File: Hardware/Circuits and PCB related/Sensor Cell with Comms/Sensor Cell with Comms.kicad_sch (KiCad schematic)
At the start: 3 parts, among them U12 STM32F103C6T6

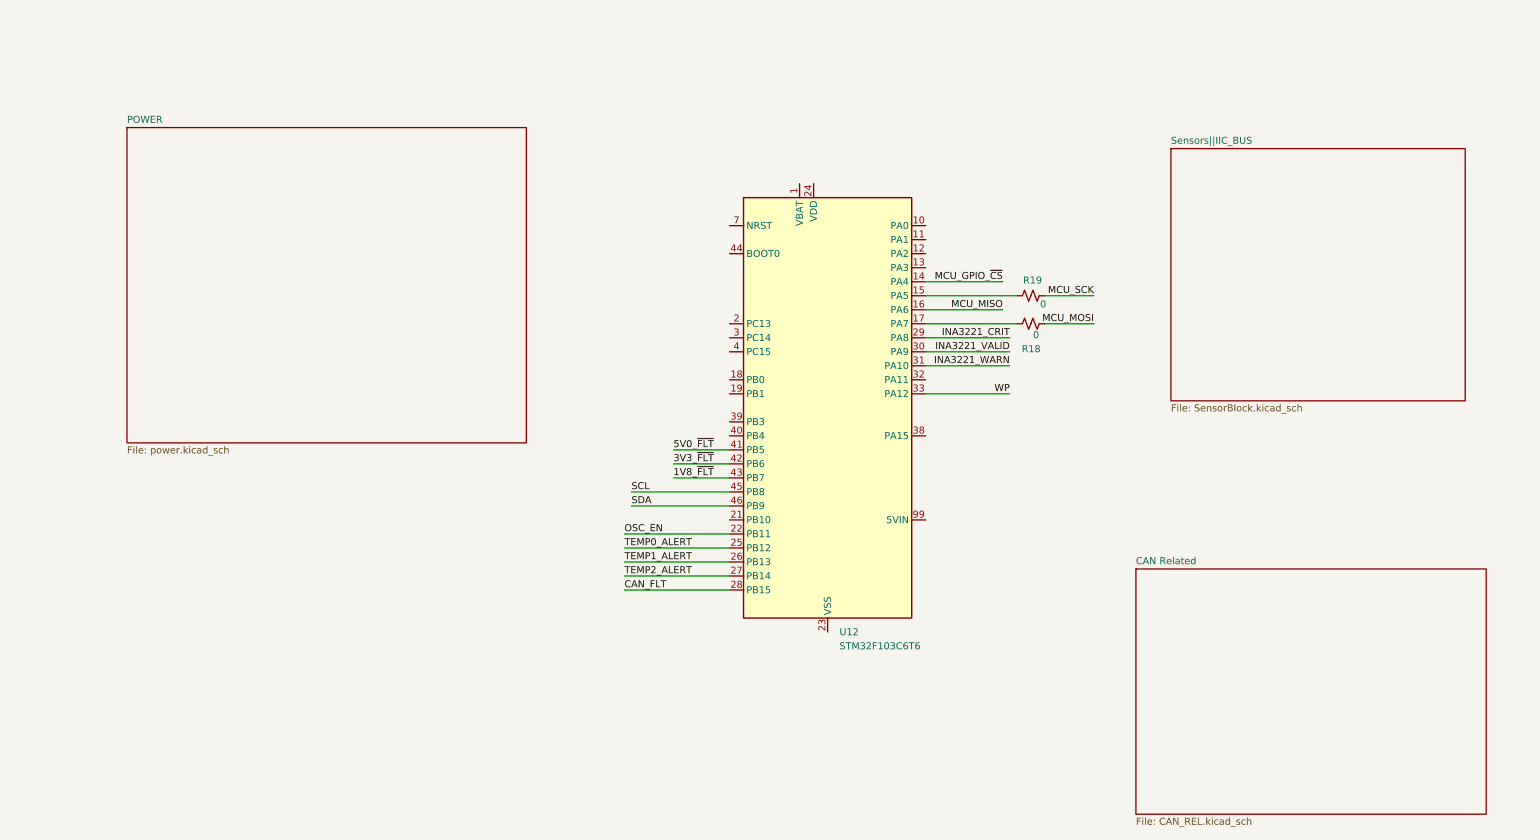
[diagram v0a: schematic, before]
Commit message: Finished schematic, added all footprints, finishing ERC now to move onto the PCB planner to have Kicad do most of the heavy lifting
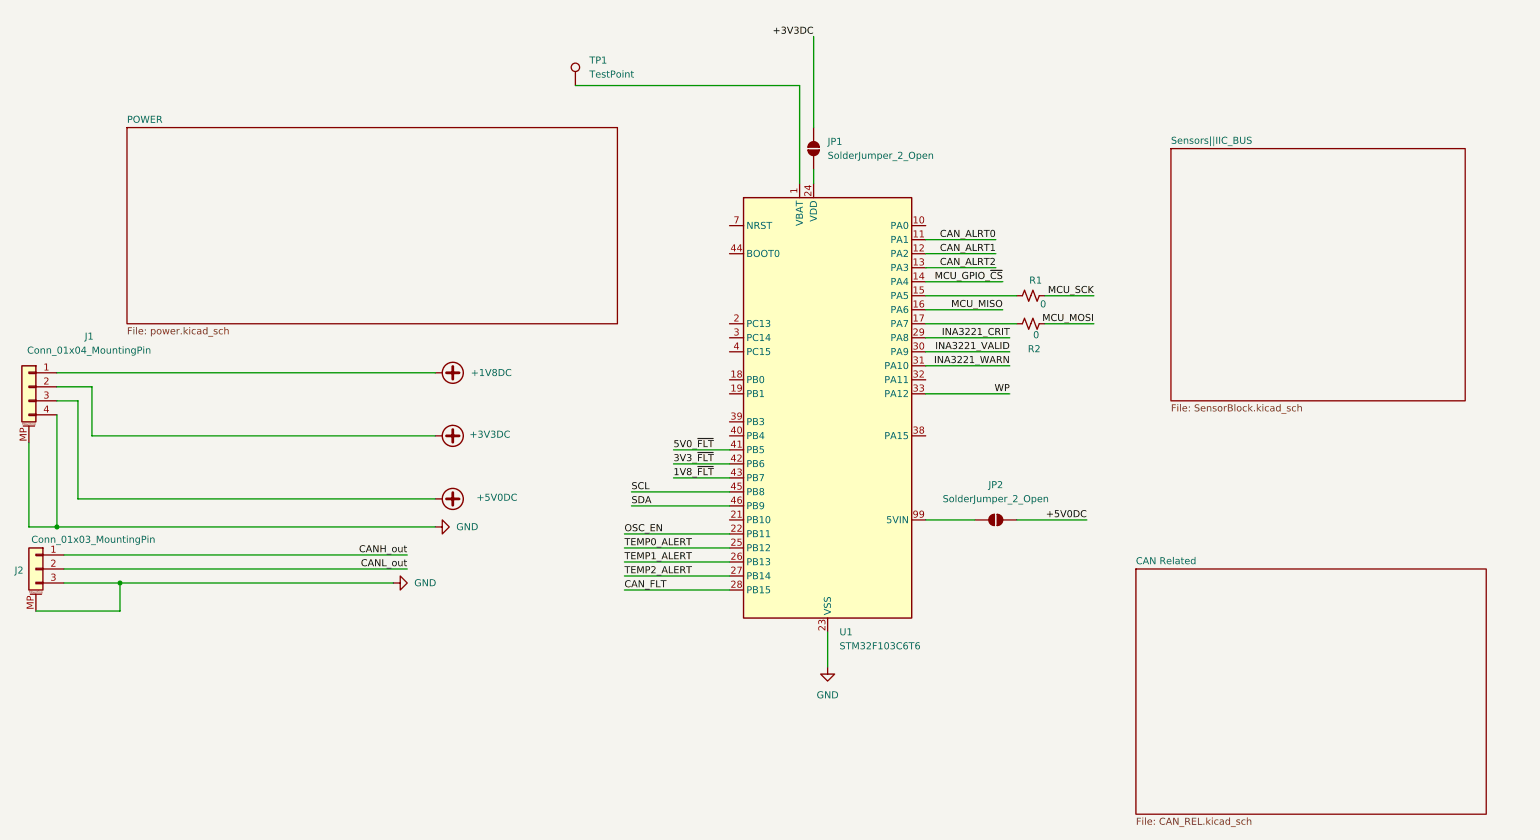
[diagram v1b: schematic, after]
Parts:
- added J1: Conn_01x04_MountingPin, Connector_Hirose:Hirose_DF57H-4P-1.2V_1x04_P1.2mm_Socket, symbol Connector_Generic_MountingPin:Conn_01x04_MountingPin
- added J2: Conn_01x03_MountingPin, Connector_Hirose:Hirose_DF57H-3P-1.2V_1x03_P1.2mm_Socket, symbol Connector_Generic_MountingPin:Conn_01x03_MountingPin
- added JP1, JP2: SolderJumper_2_Open, Jumper:SolderJumper-2_P1.3mm_Open_TrianglePad1.0x1.5mm, symbol Jumper:SolderJumper_2_Open
- added TP1: TestPoint, Connector_PinHeader_1.00mm:PinHeader_1x01_P1.00mm_Vertical, symbol Connector:TestPoint
- renumbered R19 to R1, R18 to R2, U12 to U1
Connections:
- net at U1.1 (VBAT): now also TP1.1
- net CAN_ALRT0: now reaches U1.11 (PA1)
- net CAN_ALRT1: now reaches U1.12 (PA2)
- net CAN_ALRT2: now reaches U1.13 (PA3)
- net GND: now reaches U1.23 (VSS), U1.35 (VSS), U1.47 (VSS)
- net GND: now also J1.4 (Pin_4), J1.MP (MountPin), J2.3 (Pin_3), J2.MP (MountPin)
- net at U1.24 (VDD): now also JP1.1 (A)
- net at U1.99 (5VIN): now also JP2.1 (A)
- new net +1V8DC: J1.1 (Pin_1)
- new net +3V3DC: J1.2 (Pin_2), JP1.2 (B)
- new net +5V0DC: J1.3 (Pin_3), JP2.2 (B)
- new net CANH_out: J2.1 (Pin_1)
- new net CANL_out: J2.2 (Pin_2)

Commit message: Bulk done to resolve ERC errors, went from 70 to 25. Need to resolve the remaining errors before generation of the PCB. Decided on Hirose Electric Connectors since theyre low profile and locking
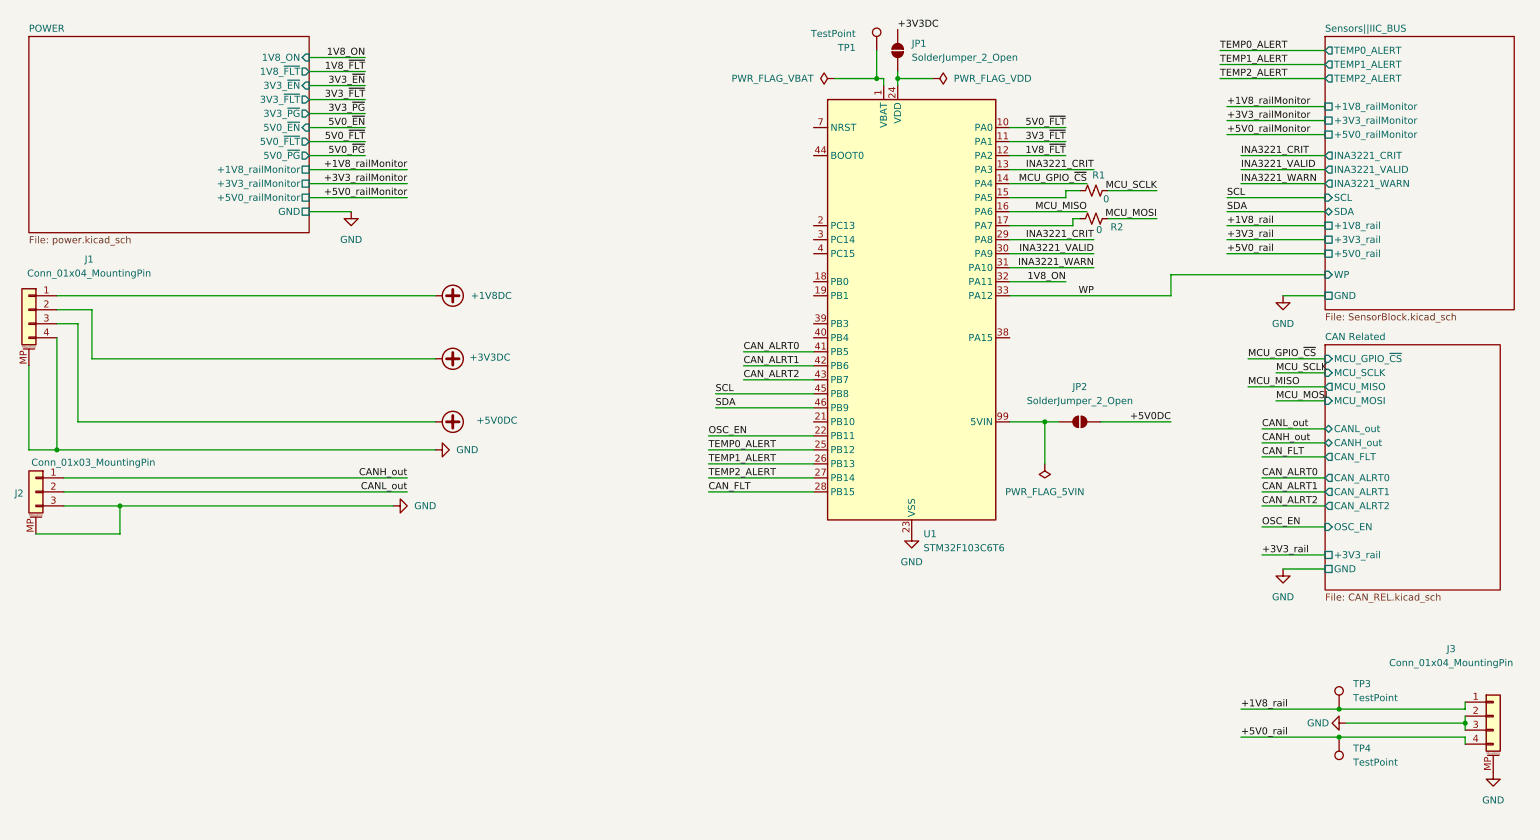
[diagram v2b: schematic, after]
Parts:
- added J3: Conn_01x04_MountingPin, Connector_Hirose:Hirose_DF57H-4P-1.2V_1x04_P1.2mm_Socket, symbol Connector_Generic_MountingPin:Conn_01x04_MountingPin
- added TP3, TP4: TestPoint, symbol Connector:TestPoint
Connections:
- net 1V8_~{FLT}: now also U1.12 (PA2); no longer U1.43 (PB7)
- net 3V3_~{FLT}: now also U1.11 (PA1); no longer U1.42 (PB6)
- net 5V0_~{FLT}: now also U1.10 (PA0); no longer U1.41 (PB5)
- net CAN_ALRT0: now also U1.41 (PB5); no longer U1.11 (PA1)
- net CAN_ALRT1: now also U1.42 (PB6); no longer U1.12 (PA2)
- net CAN_ALRT2: now also U1.43 (PB7); no longer U1.13 (PA3)
- net GND: now also J3.2 (Pin_2), J3.3 (Pin_3), J3.MP (MountPin)
- net INA3221_CRIT: now also U1.13 (PA3)
- net 1V8_ON: now reaches U1.32 (PA11)
- net MCU_SCK renamed MCU_SCLK
- new net +1V8_rail: J3.1 (Pin_1), TP3.1
- new net +5V0_rail: J3.4 (Pin_4), TP4.1
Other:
- sheet CAN Related ports: added +3V3_rail, CANH_out, CANL_out, CAN_ALRT0, CAN_ALRT1, CAN_ALRT2, CAN_FLT, GND, MCU_GPIO_~{CS}, MCU_MISO, MCU_MOSI, MCU_SCLK, OSC_EN; removed none
- sheet POWER ports: added +1V8_railMonitor, +3V3_railMonitor, +5V0_railMonitor, 1V8_ON, 1V8_~{FLT}, 3V3_~{EN}, 3V3_~{FLT}, 3V3_~{PG}, 5V0_~{EN}, 5V0_~{FLT}, 5V0_~{PG}, GND; removed none
- sheet Sensors||IIC_BUS ports: added +1V8_rail, +1V8_railMonitor, +3V3_rail, +3V3_railMonitor, +5V0_rail, +5V0_railMonitor, GND, INA3221_CRIT, INA3221_VALID, INA3221_WARN, SCL, SDA, TEMP0_ALERT, TEMP1_ALERT, TEMP2_ALERT, WP; removed none
- moved on the sheet: J1, J2, JP1, JP2, R1, R2, TP1, U1

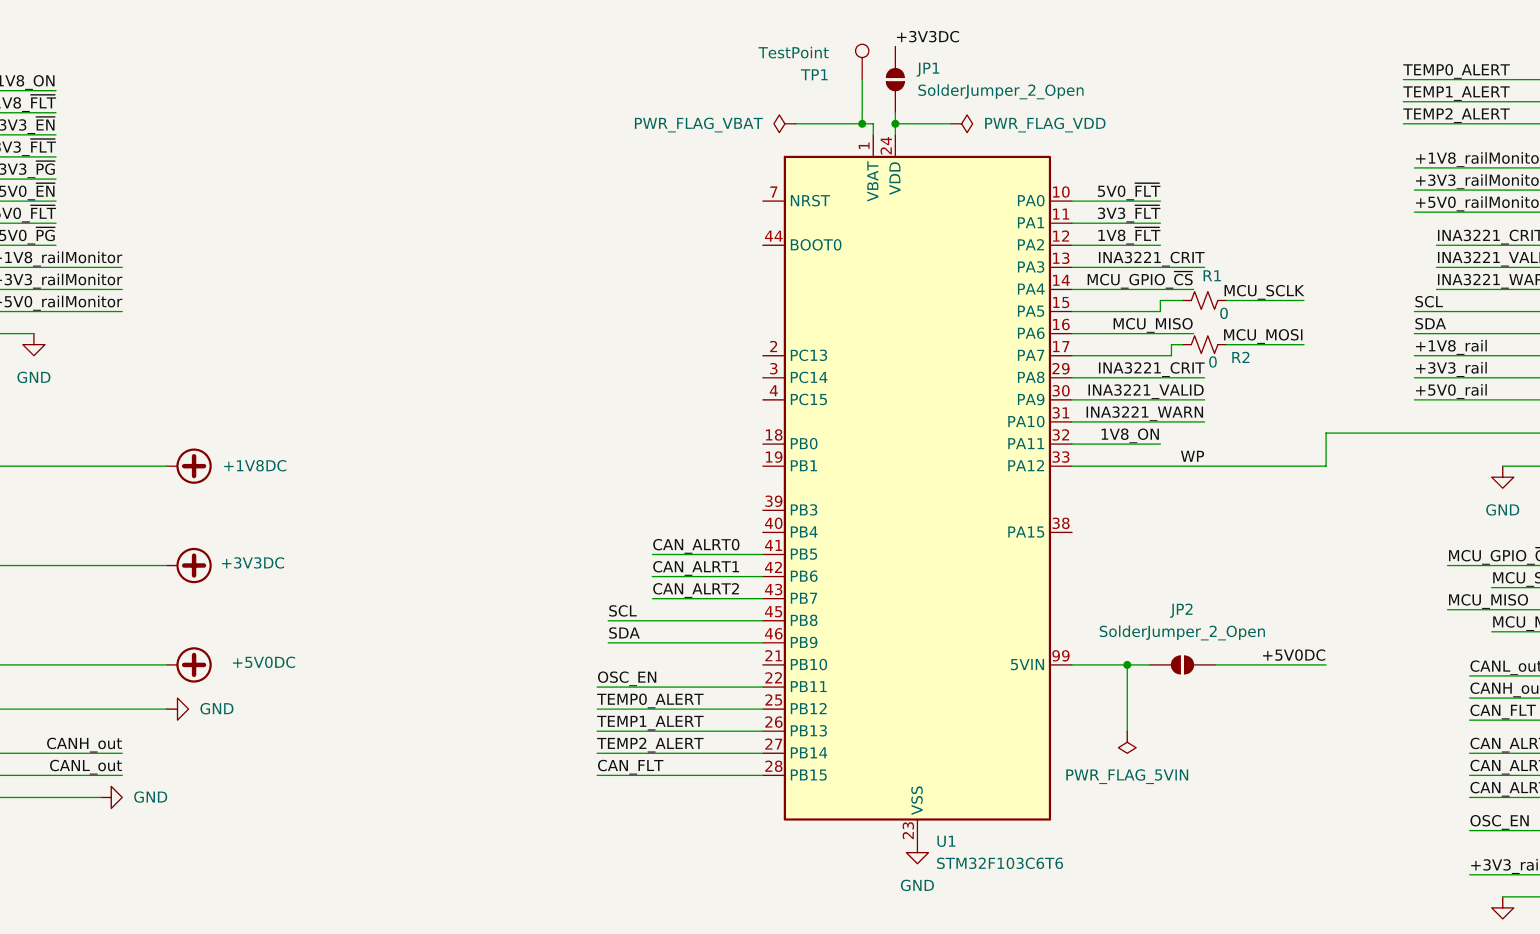
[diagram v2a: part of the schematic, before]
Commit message: Schematic done, and ERC passes successfully. Move onto PCB now that this is completed
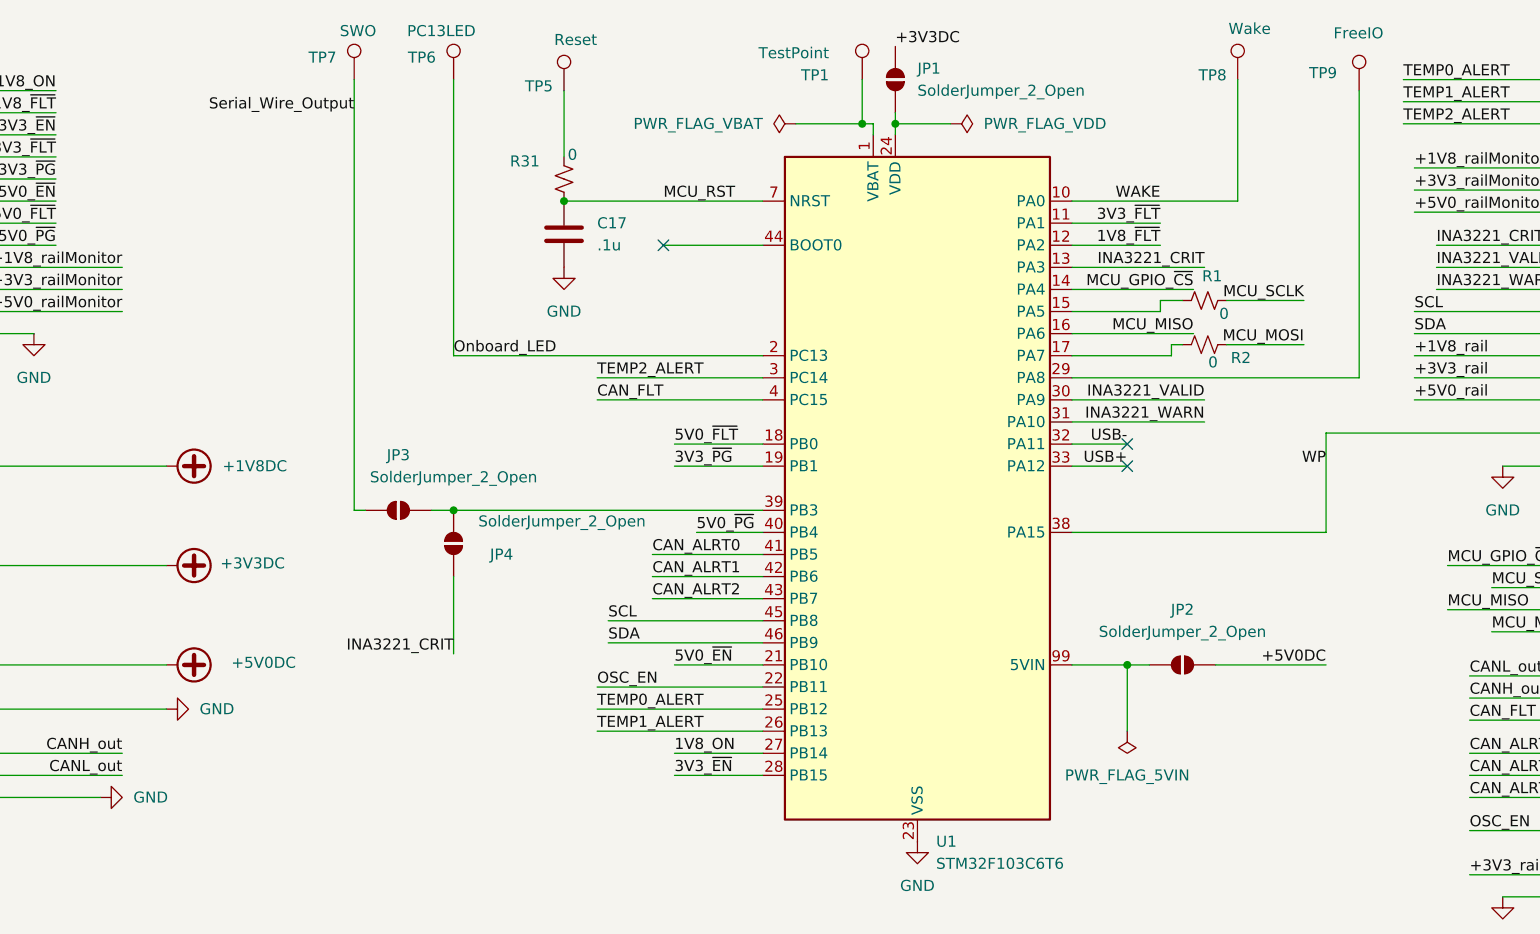
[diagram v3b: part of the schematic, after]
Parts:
- added C17: .1u, Capacitor_SMD:C_0805_2012Metric_Pad1.18x1.45mm_HandSolder, symbol Device:C
- added JP3, JP4: SolderJumper_2_Open, Jumper:SolderJumper-2_P1.3mm_Open_TrianglePad1.0x1.5mm, symbol Jumper:SolderJumper_2_Open
- added R31: 0, Resistor_SMD:R_0603_1608Metric_Pad0.98x0.95mm_HandSolder, symbol Device:R_Small_US
- added TP5: Reset, Connector_PinHeader_1.00mm:PinHeader_1x01_P1.00mm_Vertical, symbol Connector:TestPoint
- added TP6: PC13LED, Connector_PinHeader_1.00mm:PinHeader_1x01_P1.00mm_Vertical, symbol Connector:TestPoint
- added TP7: SWO, Connector_PinHeader_1.00mm:PinHeader_1x01_P1.00mm_Vertical, symbol Connector:TestPoint
- added TP8: Wake, Connector_PinHeader_1.00mm:PinHeader_1x01_P1.00mm_Vertical, symbol Connector:TestPoint
- added TP9: FreeIO, Connector_PinHeader_1.00mm:PinHeader_1x01_P1.00mm_Vertical, symbol Connector:TestPoint
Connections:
- net 1V8_ON: now also U1.27 (PB14); no longer U1.32 (PA11)
- net 3V3_~{EN}: now also U1.28 (PB15)
- net 3V3_~{PG}: now also U1.19 (PB1)
- net 5V0_~{EN}: now also U1.21 (PB10)
- net 5V0_~{FLT}: now also U1.18 (PB0); no longer U1.10 (PA0)
- net 5V0_~{PG}: now also U1.40 (PB4)
- net CAN_FLT: now also U1.4 (PC15); no longer U1.28 (PB15)
- net GND: now also C17.2
- net INA3221_CRIT: now also JP4.2 (B); no longer U1.29 (PA8)
- net TEMP2_ALERT: now also U1.3 (PC14); no longer U1.27 (PB14)
- net WP: now also U1.38 (PA15); no longer U1.33 (PA12)
- net Onboard_LED: now reaches U1.2 (PC13)
- net Onboard_LED: now also TP6.1
- net at U1.39 (PB3): now also JP3.2 (B), JP4.1 (A)
- net MCU_RST: now reaches U1.7 (NRST)
- net MCU_RST: now also C17.1, R31.2
- new net: R31.1, TP5.1
- new net: TP9.1, U1.29 (PA8)
- new net Serial_Wire_Output: JP3.1 (A), TP7.1
- new net USB+: U1.33 (PA12)
- new net USB-: U1.32 (PA11)
- new net WAKE: TP8.1, U1.10 (PA0)
- no-connect marks 0 -> 3

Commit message: First revision of PCB nearly done, Need to finish up 1v8 planes then wire components together
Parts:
- removed J1, J3: Conn_01x04_MountingPin, Connector_Hirose:Hirose_DF57H-4P-1.2V_1x04_P1.2mm_Socket, symbol Connector_Generic_MountingPin:Conn_01x04_MountingPin
- removed J2: Conn_01x03_MountingPin, Connector_Hirose:Hirose_DF57H-3P-1.2V_1x03_P1.2mm_Socket, symbol Connector_Generic_MountingPin:Conn_01x03_MountingPin
- added C22, C23: 10u, Capacitor_SMD:C_0603_1608Metric_Pad1.08x0.95mm_HandSolder, symbol Device:C
- added D3, D7: SMF5V0A, Diode_SMD:D_SMF, symbol Diode:SMF5V0A
- added D4, D6: SMF20A, Diode_SMD:D_SMF, symbol Diode:SMF20A
- added D5: SMF36A, Diode_SMD:D_SMF, symbol Diode:SMF36A
- added J1: MolexMicroFit3_1, Connector_Molex:Molex_Micro-Fit_3.0_43650-0400_1x04_P3.00mm_Horizontal, symbol Connector:Conn_01x04_Socket
- added J2: MolexMicroFit3_2, Connector_Molex:Molex_Micro-Latch_53254-0370_1x03_P2.00mm_Horizontal, symbol Connector:Conn_01x03_Socket
- added J3: MolexMicroFit3_3, Connector_Molex:Molex_Micro-Latch_53254-0370_1x03_P2.00mm_Horizontal, symbol Connector:Conn_01x03_Socket
- TP3, TP4: footprint (none) -> Connector_PinHeader_1.00mm:PinHeader_1x01_P1.00mm_Vertical
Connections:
- net +1V8DC: now also D6.1 (A1), J1.1 (Pin_1)
- net +1V8_rail: now also D4.1 (A1), J3.1 (Pin_1)
- net +3V3DC: now also D5.1 (A1), J1.2 (Pin_2)
- net +5V0DC: now also C23.2, D7.1 (A1), J1.3 (Pin_3)
- net +5V0_rail: now also D3.1 (A1), J3.3 (Pin_3)
- net CANH_out: now also J2.1 (Pin_1)
- net CANL_out: now also J2.3 (Pin_3)
- net GND: now also C22.1, C23.1, D3.2 (A2), D4.2 (A2), D5.2 (A2), D6.2 (A2), D7.2 (A2), J1.4 (Pin_4), J2.2 (Pin_2), J3.2 (Pin_2)
- net at JP1.1 (A), U1.24 (VDD): now also C22.2
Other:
- title: (none) -> MAIN Microcontroller connections
